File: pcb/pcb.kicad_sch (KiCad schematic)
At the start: 60 parts, among them J1 DC 7-30V, J2 AC current input, J3 UART, J5 USB JTAG/Serial, SW1 RESET, SW2 BOOT, U1 ESP32-S3-WROOM-1, U2 USBLC6-2SC6, U3 AMS1117-3.3, U4 AP63205WU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

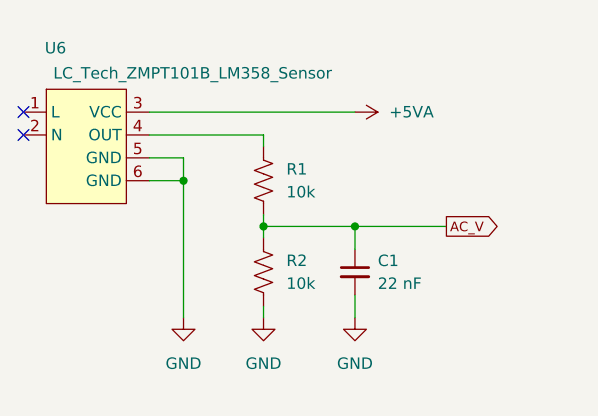
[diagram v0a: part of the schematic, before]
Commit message: Work in progress:
- Fixed AC frequency measurement error caused by inaccuracies of ADC clock
- Fixed reporting of reversed EC11 encoder rotation after replacing it with a better quality part
- Changed schematic (R1: 10k -> 4.7k) to allow more utilization of available ADC range while
  using lesser level of HW-697 hardware attenuation. This helps prevent AC_V sine wave clipping
  caused by LM358 saturation at 3.5V
- Temporary switched to a forked esp-idf-ssd1306 repository until my PR is merged to the upstream
- Added Max and Min readings of AC_V and AC_I channels at startup (debugging console)
- Display filters tweak (more latency)
- Removed fractional part from AC Voltage display (doesn't have that accuracy)
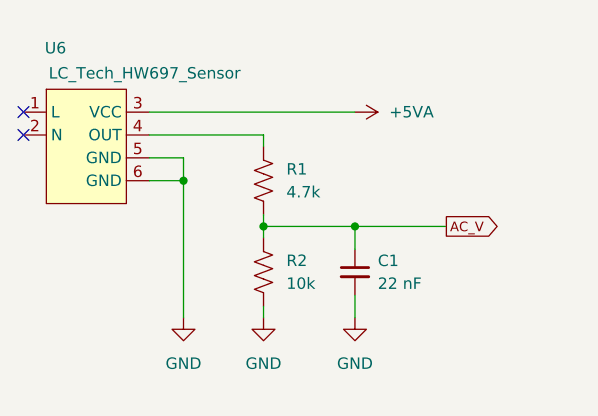
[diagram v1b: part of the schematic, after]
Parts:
- R1: value 10k -> 4.7k; LCSC C17414 -> C17673
- U6: value LC_Tech_ZMPT101B_LM358_Sensor -> LC_Tech_HW697_Sensor
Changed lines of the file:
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@@
 			)
 		)
-		(property "LTSC" ""
-			(at 139.7 116.84 0)
-			(effects
-				(font
-					(size 1.27 1.27)
-				)
-				(hide yes)
-			)
-		)
 		(pin "1"
 		)
@@
 			)
 		)
-		(property "Value" "LC_Tech_ZMPT101B_LM358_Sensor"
-			(at 39.116 22.352 0)
+		(property "Value" "LC_Tech_HW697_Sensor"
+			(at 33.782 22.352 0)
 			(effects
 				(font
@@
 			)
 		)
-		(property "Value" "10k"
+		(property "Value" "4.7k"
 			(at 49.53 35.5599 0)
 			(effects
@@
 			)
 		)
-		(property "LCSC" "C17414"
-			(at 46.99 34.29 0)
-			(effects
-				(font
-					(size 1.27 1.27)
-				)
-				(hide yes)
-			)
-		)
-		(property "LTSC" ""
+		(property "LCSC" "C17673"
 			(at 46.99 34.29 0)
 			(effects
@@
 			(at 149.86 116.84 0)
 			(effects
-				(font
-					(size 1.27 1.27)
-				)
-				(hide yes)
-			)
-		)
-		(property "LTSC" ""
-			(at 149.86 116.84 0)
-			(effects
